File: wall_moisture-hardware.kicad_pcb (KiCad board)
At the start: 4 copper layers, 78.9 x 100.7 mm, 40 parts, among them J1 Conn_01x04_Socket, J2 Conn_01x04_Socket, J3 Conn_01x03_Pin, J4 Conn_01x03_Pin, J5 490107670612, Q3 BC847,215, Q4 BSS316N, SW1 DSHP08TSGET, SW2 FSMH, U2 STM32L432KCUx, U3 TPS7A20xxxDBV, U4 TPS7A20xxxDBV, U7 OPA388IDBV, U8 AD7747, Y1 ECS-.327-7-12RR-TR

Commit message: Fix board cutt layer
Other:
- board size 78.9 x 100.7 mm -> 78.9 x 99.4 mm
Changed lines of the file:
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@@
 			(psa4output no)
 			(plot_black_and_white yes)
-			(plotinvisibletext no)
 			(sketchpadsonfab no)
 			(plotpadnumbers no)
@@
 			(layer "F.Fab")
 		)
-		(fp_text user "${REFERENCE}"
-			(at 0 0 90)
-			(layer "F.Fab")
-			(hide yes)
-			(effects
-				(font
-					(size 0.5 0.5)
-					(thickness 0.075)
-				)
-			)
-		)
 		(pad "1" smd rect
 			(at -0.7 0 90)
@@
 			(layer "F.Fab")
 		)
-		(fp_text user "${REFERENCE}"
-			(at -2.5 0 0)
-			(layer "F.Fab")
-			(hide yes)
-			(effects
-				(font
-					(size 0.4 0.4)
-					(thickness 0.06)
-				)
-			)
-		)
 		(pad "1" smd roundrect
 			(at -0.775 0 180)
@@
 			(layer "F.Fab")
 		)
-		(fp_text user "${REFERENCE}"
-			(at 0 1.5 90)
-			(layer "F.Fab")
-			(hide yes)
-			(effects
-				(font
-					(size 1 1)
-					(thickness 0.15)
-				)
-			)
-		)
 		(pad "1" smd roundrect
 			(at -3 -2.85 90)
@@
 			(layer "F.Fab")
 		)
-		(fp_text user "${REFERENCE}"
-			(at 0 0 0)
-			(layer "F.Fab")
-			(hide yes)
-			(effects
-				(font
-					(size 0.4 0.4)
-					(thickness 0.06)
-				)
-			)
-		)
 		(pad "1" smd roundrect
 			(at -1.1375 -0.95 180)
@@
 			(layer "F.Fab")
 		)
-		(fp_text user "${REFERENCE}"
-			(at 0 0 0)
-			(layer "F.Fab")
-			(hide yes)
-			(effects
-				(font
-					(size 1 1)
-					(thickness 0.15)
-				)
-			)
-		)
 		(pad "" smd roundrect
 			(at -1.15 -1.15 180)
@@
 			(layer "F.Fab")
 		)
-		(fp_text user "${REFERENCE}"
-			(at 0 0 0)
-			(layer "F.Fab")
-			(hide yes)
-			(effects
-				(font
-					(size 0.4 0.4)
-					(thickness 0.06)
-				)
-			)
-		)
 		(pad "1" smd roundrect
 			(at -1.1375 -0.95 180)
@@
 			(layer "F.Fab")
 		)
-		(fp_text user "${REFERENCE}"
-			(at 0 0 0)
-			(layer "F.Fab")
-			(hide yes)
-			(effects
-				(font
-					(size 0.4 0.4)
-					(thickness 0.06)
-				)
-			)
-		)
 		(pad "1" smd roundrect
 			(at -0.775 0 180)
@@
 	)
 	(gr_line
-		(start 361 79.537471)
-		(end 361 110.537474)
+		(start 360.571916 49.527766)
+		(end 360.571916 110)
+		(stroke
+			(width 0.05)
+			(type default)
+		)
+		(layer "Edge.Cuts")
+	)
+	(gr_line
+		(start 360.571916 110)
+		(end 373.279919 110)
 		(stroke
 			(width 0.05)
@@
 	)
 	(gr_line
-		(start 439 111.220001)
-		(end 439 79.719998)
+		(start 439 110)
+		(end 439.432984 50.048749)
 		(stroke
 			(width 0.05)
@@
 		(layer "Dwgs.User")
 		(pts
-			(xy 401.311765 8.144189) (xy 374.2265 107.575512)
+			(xy 400.365184 10.568677) (xy 374.2265 107.575512)
 		)
 		(height -64.865184)
@@
 			(keep_text_aligned yes)
 		)
-		(gr_text "99.4313 mm"
-			(at 335.296581 57.859851 90)
+		(gr_text "97.0068 mm"
+			(at 334.35 59.072095 90)
 			(layer "Dwgs.User")
 			(effects
@@
 		(layer "Dwgs.User")
 		(pts
-			(xy 373.279919 110) (xy 427.252757 110)
+			(xy 360.5 109.720001) (xy 439 110)
 		)
-		(height 21.000002)
+		(height 22.279999)
 		(orientation 0)
 		(format
@@
 			(keep_text_aligned yes)
 		)
-		(gr_text "53.9728 mm"
-			(at 400.266338 129.850002 0)
+		(gr_text "78.5000 mm"
+			(at 399.75 130.85 0)
 			(layer "Dwgs.User")
 			(effects

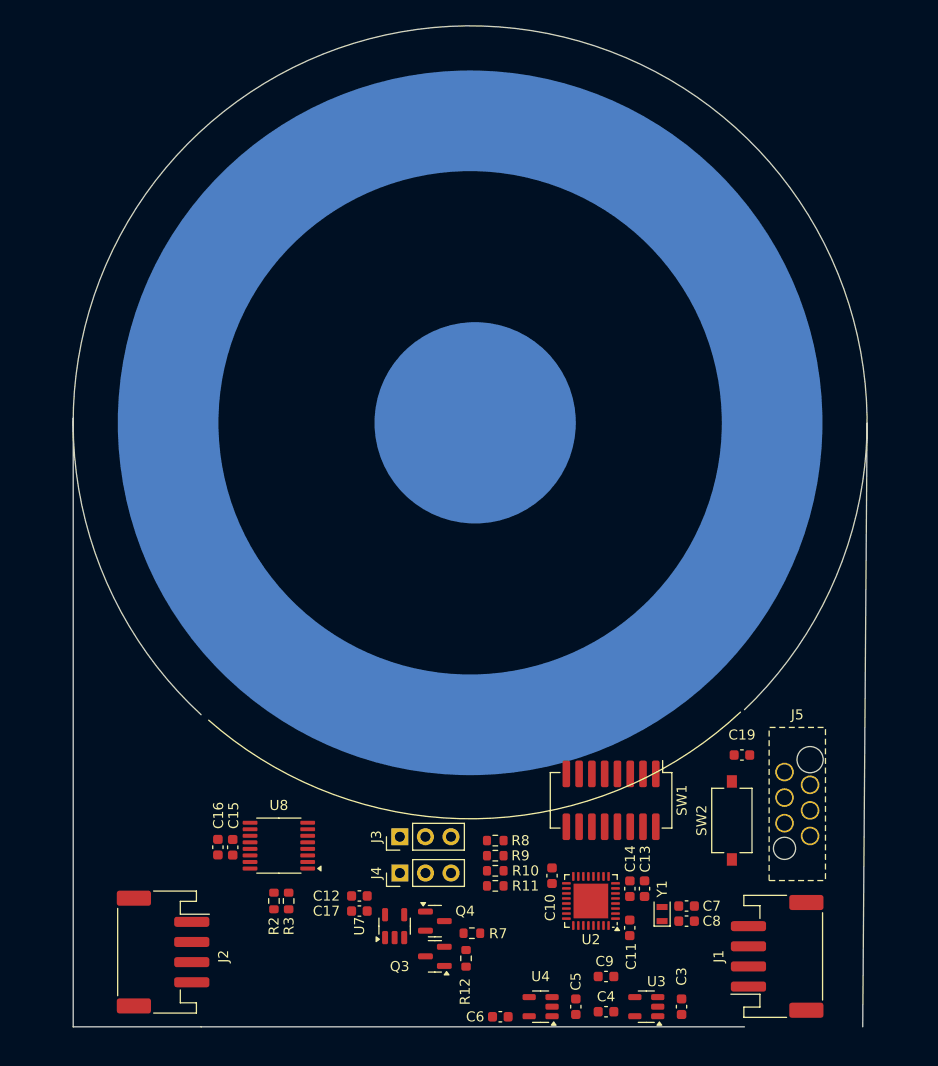
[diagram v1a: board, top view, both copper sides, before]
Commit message: design: fix board cut layer
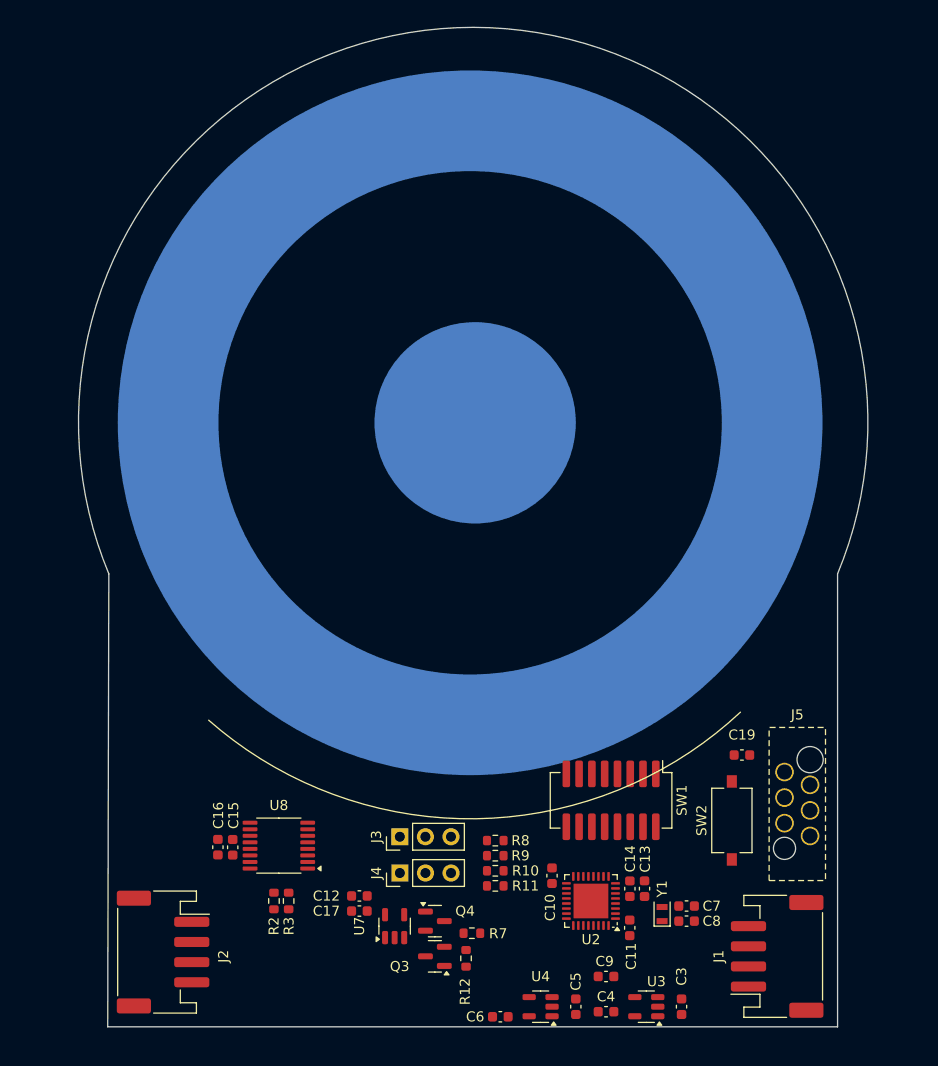
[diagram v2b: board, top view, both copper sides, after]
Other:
- board size 78.9 x 99.4 mm -> 78.4 x 99.3 mm
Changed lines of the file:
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@@
 	)
 	(gr_arc
-		(start 373.279919 78.999999)
-		(mid 399.634711 10.568677)
-		(end 427.252757 78.499999)
+		(start 364.11035 65)
+		(mid 399.212948 10.733213)
+		(end 436.5 65)
 		(stroke
 			(width 0.05)
@@
 	)
 	(gr_line
-		(start 360.571916 49.527766)
-		(end 360.571916 110)
+		(start 364.11035 64.999997)
+		(end 364 110)
 		(stroke
 			(width 0.05)
@@
 	)
 	(gr_line
-		(start 360.571916 110)
-		(end 373.279919 110)
+		(start 364 110)
+		(end 436.5 110)
 		(stroke
 			(width 0.05)
@@
 	)
 	(gr_line
-		(start 373.279919 110)
-		(end 427.252757 110)
-		(stroke
-			(width 0.05)
-			(type default)
-		)
-		(layer "Edge.Cuts")
-	)
-	(gr_line
-		(start 439 110)
-		(end 439.432984 50.048749)
+		(start 436.5 110)
+		(end 436.5 64.999997)
 		(stroke
 			(width 0.05)
@@
 		(layer "Dwgs.User")
 		(pts
-			(xy 400.365184 10.568677) (xy 374.2265 107.575512)
+			(xy 400.365184 10.568677) (xy 364 110)
 		)
 		(height -64.865184)
@@
 			(keep_text_aligned yes)
 		)
-		(gr_text "97.0068 mm"
-			(at 334.35 59.072095 90)
+		(gr_text "99.4313 mm"
+			(at 334.35 60.284339 90)
 			(layer "Dwgs.User")
 			(effects
@@
 		(layer "Dwgs.User")
 		(pts
-			(xy 427.252754 78.499999) (xy 427.252757 110)
+			(xy 427.252754 78.499999) (xy 436.5 110)
 		)
 		(height 28.247246)
@@
 		(layer "Dwgs.User")
 		(pts
-			(xy 360.5 109.720001) (xy 439 110)
+			(xy 364 110) (xy 436.5 110)
 		)
 		(height 22.279999)
@@
 			(keep_text_aligned yes)
 		)
-		(gr_text "78.5000 mm"
-			(at 399.75 130.85 0)
+		(gr_text "72.5000 mm"
+			(at 400.25 131.129999 0)
 			(layer "Dwgs.User")
 			(effects

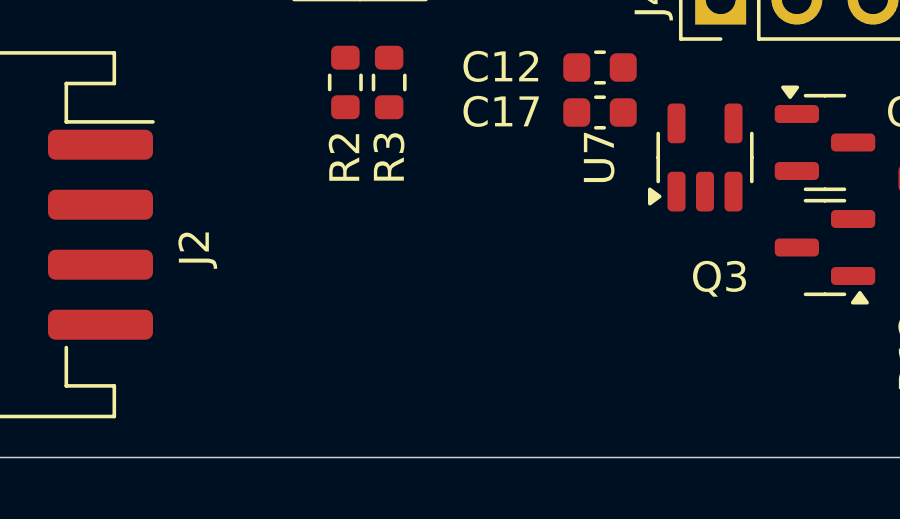
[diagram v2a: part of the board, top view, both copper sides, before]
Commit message: silk: add board name and placeholder to version number
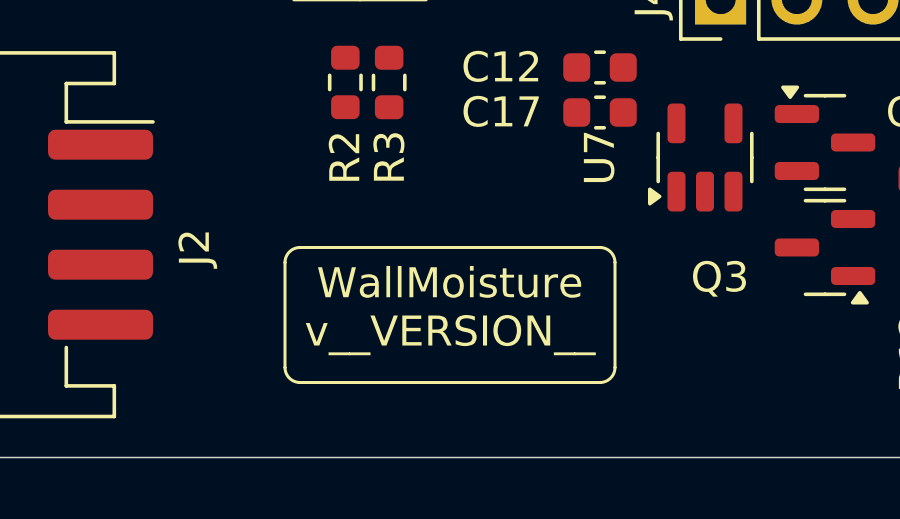
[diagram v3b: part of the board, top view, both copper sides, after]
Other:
- board text added: "WallMoisture v__VERSION__"
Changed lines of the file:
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@@
 		(embedded_fonts no)
+	)
+	(gr_line
+		(start 389.5 103.5)
+		(end 389.5 107)
+		(stroke
+			(width 0.1)
+			(type default)
+		)
+		(layer "F.SilkS")
+	)
+	(gr_arc
+		(start 378.5 103.5)
+		(mid 378.646447 103.146447)
+		(end 379 103)
+		(stroke
+			(width 0.1)
+			(type default)
+		)
+		(layer "F.SilkS")
+	)
+	(gr_arc
+		(start 389 103)
+		(mid 389.353553 103.146447)
+		(end 389.5 103.5)
+		(stroke
+			(width 0.1)
+			(type default)
+		)
+		(layer "F.SilkS")
+	)
+	(gr_line
+		(start 389 103)
+		(end 379 103)
+		(stroke
+			(width 0.1)
+			(type default)
+		)
+		(layer "F.SilkS")
+	)
+	(gr_line
+		(start 389 107.5)
+		(end 379 107.5)
+		(stroke
+			(width 0.1)
+			(type default)
+		)
+		(layer "F.SilkS")
 	)
 	(gr_arc
@@
 			(width 0.1)
 			(type solid)
+		)
+		(layer "F.SilkS")
+	)
+	(gr_line
+		(start 378.5 107)
+		(end 378.5 103.5)
+		(stroke
+			(width 0.1)
+			(type default)
+		)
+		(layer "F.SilkS")
+	)
+	(gr_arc
+		(start 389.5 107)
+		(mid 389.353553 107.353553)
+		(end 389 107.5)
+		(stroke
+			(width 0.1)
+			(type default)
+		)
+		(layer "F.SilkS")
+	)
+	(gr_arc
+		(start 379 107.5)
+		(mid 378.646447 107.353553)
+		(end 378.5 107)
+		(stroke
+			(width 0.1)
+			(type default)
 		)
 		(layer "F.SilkS")
@@
 		(layer "Edge.Cuts")
 	)
+	(gr_text "WallMoisture\nv__VERSION__"
+		(at 384 105 0)
+		(layer "F.SilkS")
+		(effects
+			(font
+				(size 1 1)
+				(thickness 0.1)
+			)
+		)
+	)
 	(dimension

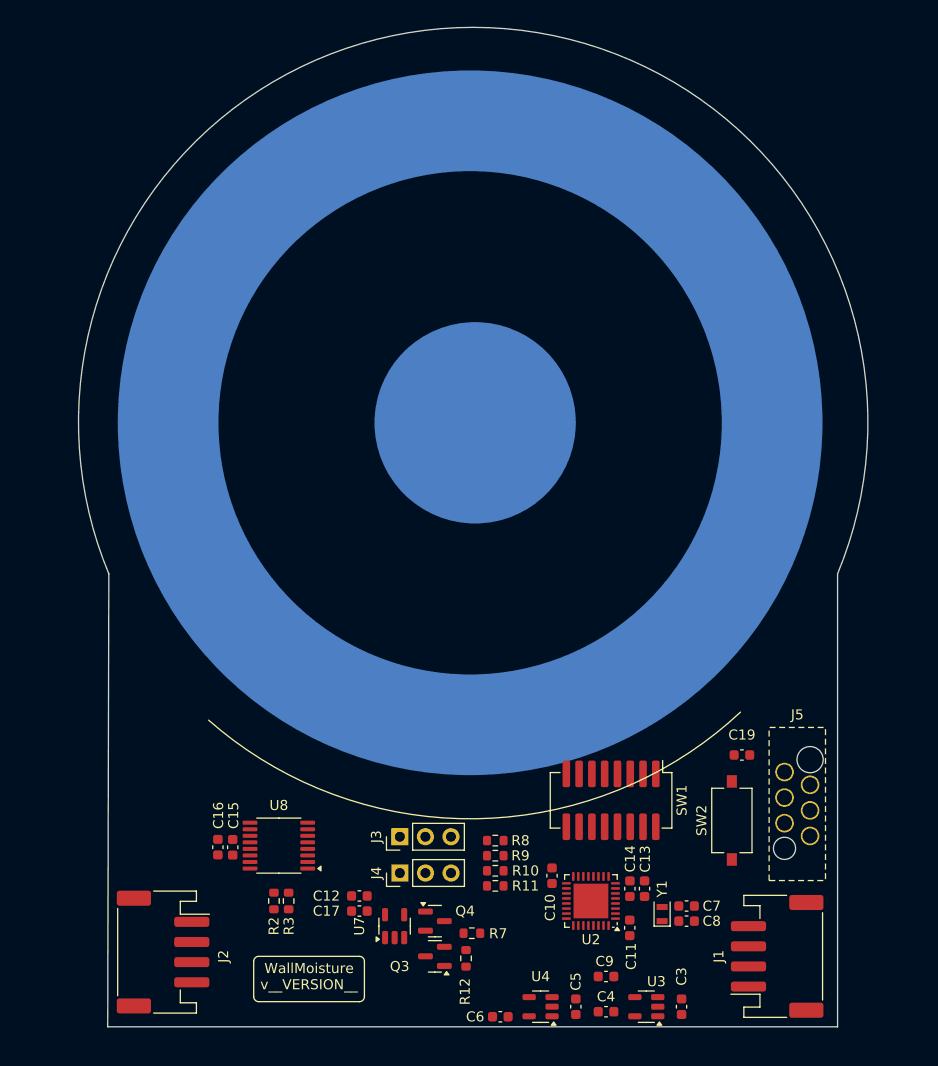
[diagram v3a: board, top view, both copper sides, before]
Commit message: design: fix some rules check
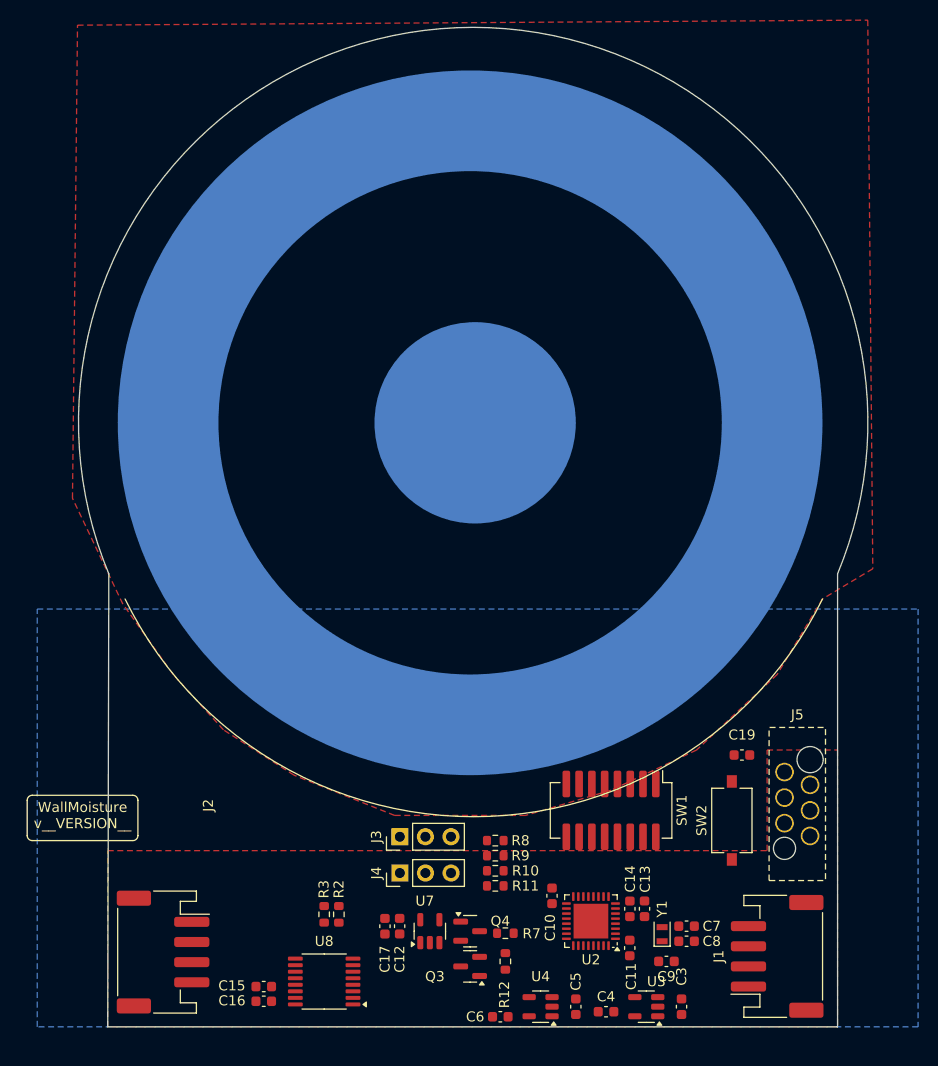
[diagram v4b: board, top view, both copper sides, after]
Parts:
- moved C16 16.0 mm to (379.5, 107.5), turned to 180 degrees
- moved U8 14.2 mm to (385.5, 105.5)
- moved C15 14.2 mm to (379.5, 106.0), turned to 180 degrees
- moved R2 6.58 mm to (387.0, 98.8), turned to -90 degrees
- moved C9 6.18 mm to (419.5, 103.5), turned to 0 degrees
- moved C12 5.00 mm to (393.0, 100.0), turned to -90 degrees
- moved R12 3.92 mm to (403.5, 103.5)
- moved R3 3.77 mm to (385.5, 98.8), turned to -90 degrees
- moved Q3 3.64 mm to (400.0, 104.0)
- moved Q4 3.64 mm to (400.0, 100.5)
- moved U7 3.54 mm to (396.0, 100.5)
- moved R7 3.32 mm to (403.5, 100.7)
- moved C17 2.95 mm to (391.5, 100.0), turned to -90 degrees
- moved C10 2.00 mm to (408.1, 97.0)
- moved C11 2.00 mm to (415.9, 102.2)
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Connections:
- net /Connector and Power/5V renamed +5V
- net Net-(J4-Pin_2) renamed /Analog frontend/SENSOR_SHIELD
- Q3 pad 1: Net-(Q3-C) -> Net-(Q3-B)
- Q3 pad 2: Net-(Q3-B) -> GND
- Q3 pad 3: GND -> Net-(Q3-C)
- U8 pad 4: (no net) -> unconnected-(U8-NC-Pad4)
- U8 pad 7: /µC and digital/AD7747_CIN- -> unconnected-(U8-CIN1--Pad7)
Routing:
- added copper zone on B.Cu, net /Analog frontend/SENSOR_SHIELD
- added copper zone on F.Cu, net /Analog frontend/SENSOR_SHIELD
- added copper zone on F.Cu, net GND
